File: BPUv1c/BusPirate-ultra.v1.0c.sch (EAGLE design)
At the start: 193 parts, among them J1 USB-C-12, J2 CON_HEADER_1X04, J3 CON_HEADER_1X10-RIGHT_ANGLED_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, J4 CON_MOLEX_MALE_SMT_SH_1.25, Q300 PMV65XP, Q301 DMMT3906W, U100 STM32F103ZX, U101 W25X40CL, U200 74HCT4067, U201 MCP6001, U202 ADS7041, U300 MCP1824_ADJ, U301 MCP6001, U302 MCP1700, U303 MCP1801T-1202I/OT, U400 SN74LVC1T45DBV, U401 SN74LVC1T45DBV, U402 74LVC1G07DBV, U403 74LVC1G07DBV, U404 SN74LVC1T45DBV, U405 SN74LVC1T45DBV, U406 74LVC1G07DBV, U407 74LVC1G07DBV, U408 SN74LVC1T45DBV, U409 SN74LVC1T45DBV, U410 74LVC1G07DBV, U411 74LVC1G07DBV, U412 SN74LVC1T45DBV, U413 SN74LVC1T45DBV, U414 74LVC1G07DBV, U415 74LVC1G07DBV, U500 74HCT4066PW, U501 74HCT4066PW, U600 23LC1024, U601 23LC1024, U602 74LVC245A, U700 ICE40HX4K

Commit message: continue on v1c schematic revisions -removed net DISPLAY_CSI on MCU pin 49 -renamed MCU_AUX5 to MCU_AUX4 and MCU_AUX6 to MCU_AUX5 -renamed MCU_ADC5 to MCU_ADC2 -renamed MCU_ADC6 to MCU_ADC3 -wired MCU_ADC0 to PA0 probing U300 output, with 2 voltage divider resistors
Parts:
- added R310, R311: 10K, dp_devices.v6:RESISTOR-0603
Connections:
- net MCU_ADC5 renamed MCU_ADC3
- net MCU_ADC6 renamed MCU_ADC2
- removed net DISPLAY_CSI: U100U.FSMC_NIOS16/FT/PF11
- removed net MCU_AUX6: U100U.TIM4_CH4('0')/I2C1_SDA('1')/FT/PB9, U700BANK0.IOT_192
- new net MCU_ADC0: R310.2, R311.1, U100U.PA0/WKUP/USART2_CTS('0')/ADC123_IN0/TIM2_CH1_ETR/TIM5_CH1/TIM8_ETR
- new net MCU_AUX4: U100U.TIM4_CH3('0')/I2C1_SCL('1')/FT/PB8, U700BANK0.IOT_206
- net GND: now also R311.2
- net MCU_AUX5: now also U100U.TIM4_CH4('0')/I2C1_SDA('1')/FT/PB9, U700BANK0.IOT_192; no longer U100U.TIM4_CH3('0')/I2C1_SCL('1')/FT/PB8, U700BANK0.IOT_206
- net N$26: now also R310.1
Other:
- moved on the sheet: C301, Q300, Q301, Q301B, R302, R303, R304, R305

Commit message: finishing up routing on v1c board
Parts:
- C100, C101, C102, C103, C106, C108, C109, C110, C111, C112, C114, C200, C201, C202, C203, C204, C205, C302, C303, C308, C501, C602, C702, C703, C704, C705, C707, C709, C711, C712, C713, C714, C715: device dp_devices.v6:CAPACITOR_NPOL-0603 -> dp_devices.v6:CAPACITOR_NPOL-0402
- R100, R200, R201, R202, R203, R204, R300, R301, R307, R308, R309, R310, R311, R700, R701, R702, R800, R801, R802, R803, R804, R805, R806: device dp_devices.v6:RESISTOR-0603 -> dp_devices.v6:RESISTOR-0402
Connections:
- net ADC_CLOCK: now also U700BANK2.IOB_80; no longer U700BANK2.IOB_79
- net ADC_DATA: now also U700BANK2.IOB_79; no longer U700BANK2.IOB_80

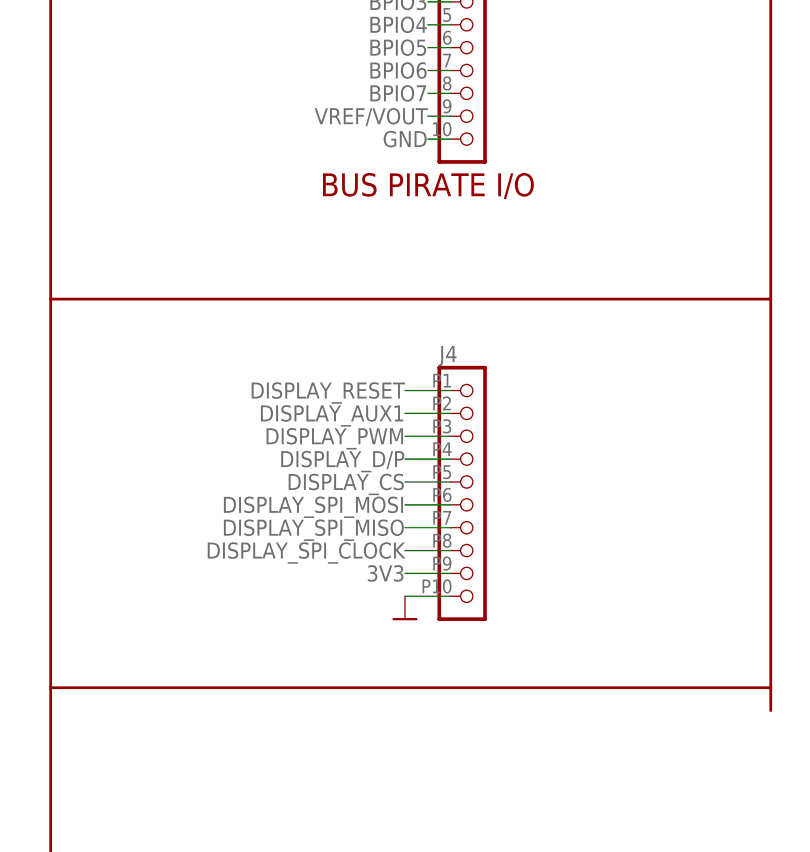
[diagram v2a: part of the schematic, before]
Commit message: change display connector to FPC connector, done routing
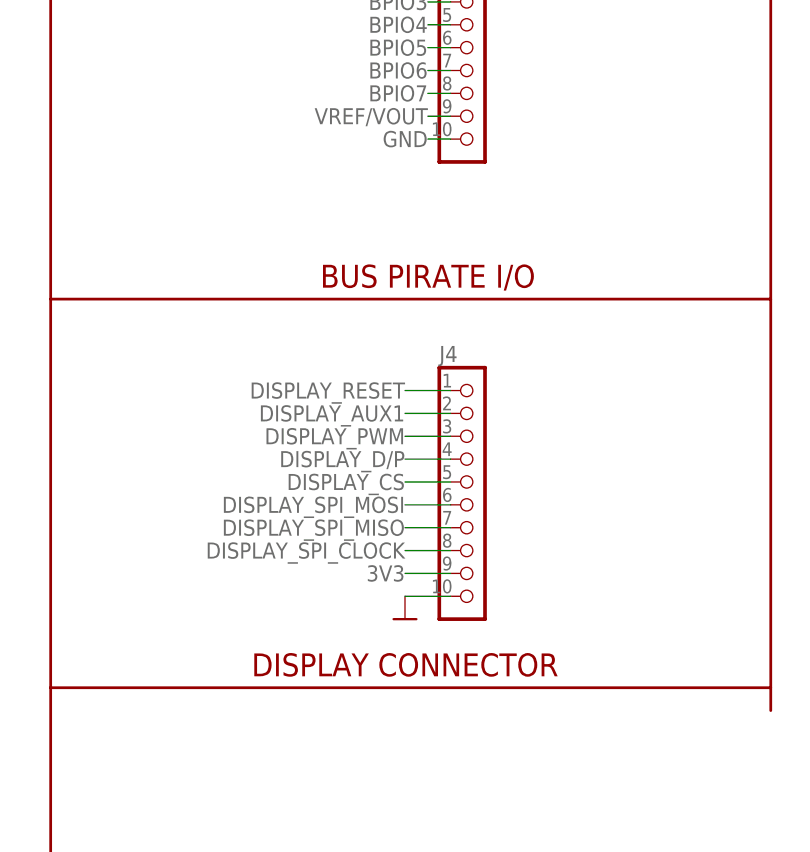
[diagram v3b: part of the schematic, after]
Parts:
- J4: value CON_MOLEX_MALE_SMT_SH_1.25 -> CON-FPC_X05B20L10T; device dp_devices.v6:CON_MOLEX_MALE_SMT_SH_1.25 -> dp_devices.v6:CON-FPC_X05B20L10T
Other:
- note added: "DISPLAY CONNECTOR"
- moved on the sheet: J4
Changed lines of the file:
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@@
 <part name="U501" library="dp_devices.v6" deviceset="IC_74HCT4066PW" device="" value="74HCT4066PW"/>
 <part name="U602" library="dp_devices.v6" deviceset="IC_BUFF_74LVC245A" device="-TSSOP20" value="74LVC245A"/>
-<part name="J4" library="dp_devices.v6" deviceset="CON_MOLEX_MALE_SMT_SH_1.25" device=""/>
 <part name="GND83" library="dp_devices.v6" deviceset="SUPPLY_GND" device=""/>
 <part name="J1" library="usbc" deviceset="USB-C-12" device=""/>
@@
 <part name="R311" library="dp_devices.v6" deviceset="RESISTOR" device="-0402" value="10K"/>
 <part name="GND40" library="dp_devices.v6" deviceset="SUPPLY_GND" device=""/>
+<part name="J4" library="dp_devices.v6" deviceset="CON-FPC_X05B20L10T" device=""/>
 </parts>
 <sheets>
@@
 <text x="317.5" y="200.66" size="2.54" layer="94" ratio="10" align="center">SRAMS</text>
 <text x="157.48" y="5.08" size="2.54" layer="94" ratio="10" align="center">IO BUFFER/GATE</text>
-<text x="708.66" y="91.44" size="2.54" layer="94" ratio="10" align="center">BUS PIRATE I/O</text>
+<text x="708.66" y="81.28" size="2.54" layer="94" ratio="10" align="center">BUS PIRATE I/O</text>
 <text x="795.02" y="189.23" size="2.54" layer="94" ratio="10" align="center">PWR</text>
 <text x="797.56" y="148.59" size="2.54" layer="94" ratio="10" align="center">MODE</text>
@@
 ADC_MUX_EN to FPGA</text>
 <text x="60.96" y="469.9" size="1.778" layer="91" align="center-right">ADC for 1.2V</text>
+<text x="706.12" y="38.1" size="2.54" layer="94" ratio="10" align="center">DISPLAY CONNECTOR</text>
 </plain>
 <instances>
@@
 <instance part="U602" gate="G$1" x="327.66" y="93.98"/>
 <instance part="U602" gate="SUPPLY" x="497.84" y="327.66"/>
-<instance part="J4" gate="J" x="711.2" y="55.88"/>
 <instance part="GND83" gate="G$1" x="706.12" y="43.18" smashed="yes"/>
 <instance part="J1" gate="G$1" x="607.06" y="160.02" rot="MR0"/>
@@
 </instance>
 <instance part="GND40" gate="G$1" x="368.3" y="279.4" smashed="yes"/>
+<instance part="J4" gate="J" x="711.2" y="55.88"/>
 </instances>
 <busses>
@@
 </segment>
 <segment>
-<pinref part="J4" gate="J" pin="10"/>
 <wire x1="711.2" y1="45.72" x2="706.12" y2="45.72" width="0.1524" layer="91"/>
 <pinref part="GND83" gate="G$1" pin="GND"/>
+<pinref part="J4" gate="J" pin="10"/>
 </segment>
 <segment>
@@
 </segment>
 <segment>
-<pinref part="J4" gate="J" pin="9"/>
 <wire x1="711.2" y1="48.26" x2="706.12" y2="48.26" width="0.1524" layer="91"/>
 <label x="706.12" y="48.26" size="1.778" layer="95" align="center-right"/>
+<pinref part="J4" gate="J" pin="9"/>
 </segment>
 <segment>
@@
 </segment>
 </net>
-<net name="N$26" class="0">
+<net name="N$26" class="1">
 <segment>
 <wire x1="355.6" y1="327.66" x2="358.14" y2="327.66" width="0.1524" layer="91"/>
@@
 </segment>
 </net>
-<net name="DISPLAY_SPI_CLOCK" class="0">
+<net name="DISPLAY_SPI_CLOCK" class="3">
 <segment>
 <pinref part="U100" gate="U" pin="PA5/SPI1_SCK('0')/ADC12_IN5"/>
@@
 </segment>
 <segment>
-<pinref part="J4" gate="J" pin="8"/>
 <wire x1="711.2" y1="50.8" x2="706.12" y2="50.8" width="0.1524" layer="91"/>
 <label x="706.12" y="50.8" size="1.778" layer="95" align="center-right"/>
+<pinref part="J4" gate="J" pin="8"/>
 </segment>
 </net>
-<net name="DISPLAY_SPI_MOSI" class="0">
+<net name="DISPLAY_SPI_MOSI" class="3">
 <segment>
 <pinref part="U100" gate="U" pin="PA7/SPI1_MOSI('0')/TIM8_CH1N/ADC12_IN7/TIM3_CH2('00')/TIM1_CH1N('01')"/>
@@
 </segment>
 <segment>
-<pinref part="J4" gate="J" pin="6"/>
 <wire x1="711.2" y1="55.88" x2="706.12" y2="55.88" width="0.1524" layer="91"/>
 <label x="706.12" y="55.88" size="1.778" layer="95" align="center-right"/>
+<pinref part="J4" gate="J" pin="6"/>
 </segment>
 </net>
-<net name="DISPLAY_SPI_MISO" class="0">
+<net name="DISPLAY_SPI_MISO" class="3">
 <segment>
 <pinref part="U100" gate="U" pin="PA6/SPI1_MISO('0')/TIM8_BKIN/ADC12_IN6/TIM3_CH1('00')/TIM1_BKIN('01')"/>
@@
 </segment>
 <segment>
-<pinref part="J4" gate="J" pin="7"/>
 <wire x1="711.2" y1="53.34" x2="706.12" y2="53.34" width="0.1524" layer="91"/>
 <label x="706.12" y="53.34" size="1.778" layer="95" align="center-right"/>
+<pinref part="J4" gate="J" pin="7"/>
 </segment>
 </net>
@@
 </segment>
 </net>
-<net name="DISPLAY_AUX1" class="0">
+<net name="DISPLAY_AUX1" class="3">
 <segment>
-<pinref part="J4" gate="J" pin="2"/>
 <wire x1="711.2" y1="66.04" x2="706.12" y2="66.04" width="0.1524" layer="91"/>
 <label x="706.12" y="66.04" size="1.778" layer="95" align="center-right"/>
+<pinref part="J4" gate="J" pin="2"/>
 </segment>
 <segment>
@@
 </segment>
 </net>
-<net name="DISPLAY_PWM" class="0">
+<net name="DISPLAY_PWM" class="3">
 <segment>
 <pinref part="U100" gate="U" pin="ADC12_IN8/TIM3_CH3('00'OR'10')/TIM8_CH2N/TIM1_CH2N('01')/PB0"/>
@@
 </segment>
 <segment>
-<pinref part="J4" gate="J" pin="3"/>
 <wire x1="711.2" y1="63.5" x2="706.12" y2="63.5" width="0.1524" layer="91"/>
 <label x="706.12" y="63.5" size="1.778" layer="95" align="center-right"/>
+<pinref part="J4" gate="J" pin="3"/>
 </segment>
 </net>
@@
 </segment>
 </net>
-<net name="DISPLAY_D/P" class="0">
+<net name="DISPLAY_D/P" class="3">
 <segment>
-<pinref part="J4" gate="J" pin="4"/>
 <wire x1="711.2" y1="60.96" x2="706.12" y2="60.96" width="0.1524" layer="91"/>
 <label x="706.12" y="60.96" size="1.778" layer="95" align="center-right"/>
+<pinref part="J4" gate="J" pin="4"/>
 </segment>
 <segment>
@@
 </segment>
 </net>
-<net name="DISPLAY_CS" class="0">
+<net name="DISPLAY_CS" class="3">
 <segment>
-<pinref part="J4" gate="J" pin="5"/>
 <wire x1="711.2" y1="58.42" x2="706.12" y2="58.42" width="0.1524" layer="91"/>
 <label x="706.12" y="58.42" size="1.778" layer="95" align="center-right"/>
+<pinref part="J4" gate="J" pin="5"/>
 </segment>
 <segment>
@@
 </segment>
 </net>
-<net name="DISPLAY_RESET" class="0">
+<net name="DISPLAY_RESET" class="3">
 <segment>
-<pinref part="J4" gate="J" pin="1"/>
 <wire x1="711.2" y1="68.58" x2="706.12" y2="68.58" width="0.1524" layer="91"/>
 <label x="706.12" y="68.58" size="1.778" layer="95" align="center-right"/>
+<pinref part="J4" gate="J" pin="1"/>
 </segment>
 <segment>
